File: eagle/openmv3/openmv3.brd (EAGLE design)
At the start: 35.6 x 44.5 mm, 60 parts, among them Q1 MOSFET, U1 STM32F765VGT6, U2 OV7725, U3 BD33IA, X1 47571-0001, X2 MICROUSB-RIGHT, Y1 7S-12.000MAHE-T

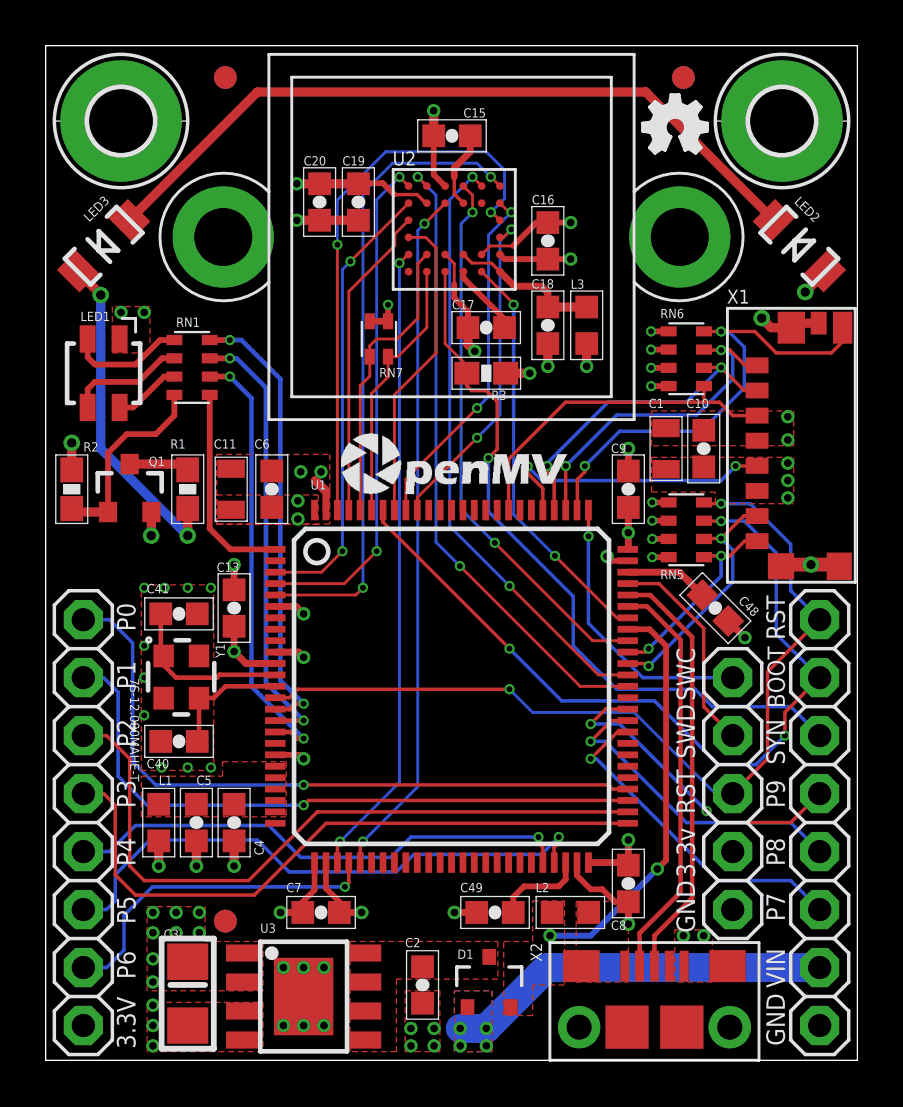
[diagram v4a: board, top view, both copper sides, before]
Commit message: Update OMV3 Eagle files.
* Add 22uF for the uSD
* Add 22uf for reg input
* Add 47uF near the MCU
* Add 47uF near the sensor
* Add 22uF for sensor digital input
* Replace sensor bead with RC filter on AVDD
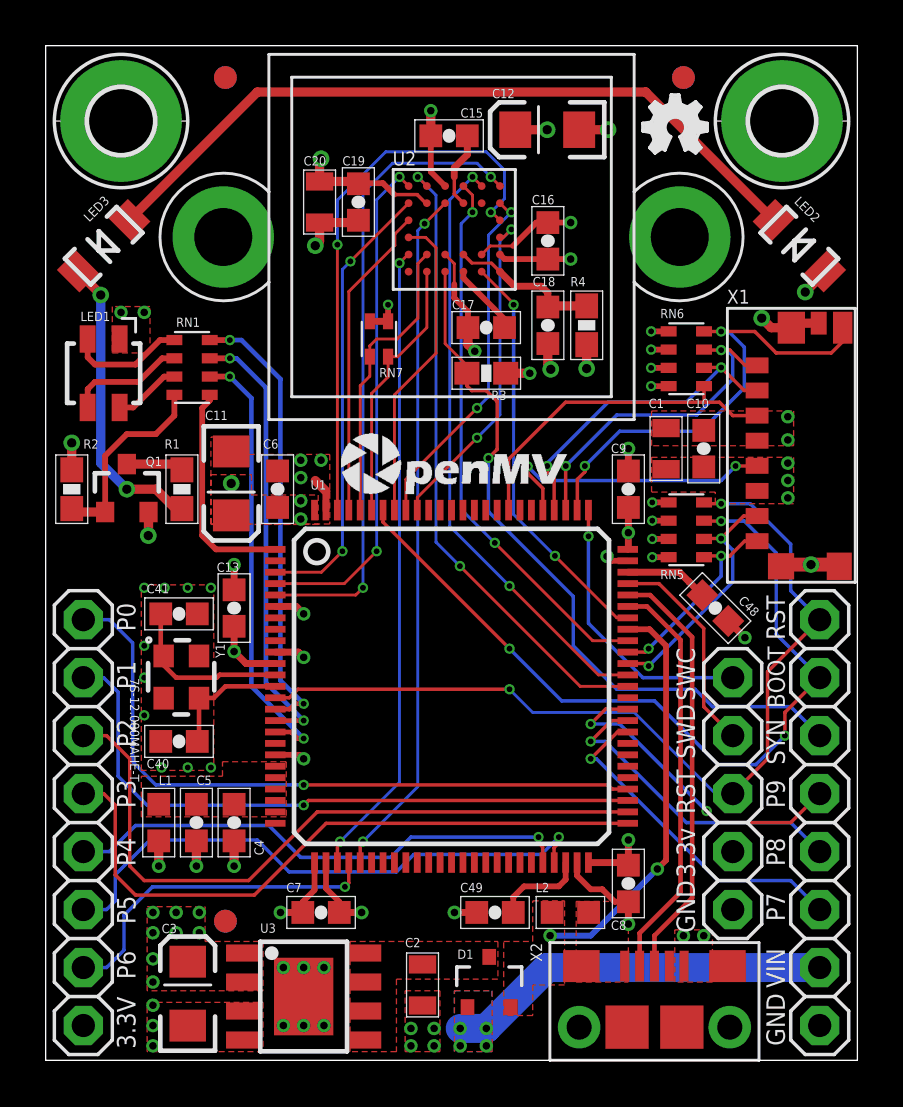
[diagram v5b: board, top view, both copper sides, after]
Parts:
- removed L3: MPZ1608S181ATAH0, sfe:0603
- added C12: 47uF, sfe:EIA3216
- added R4: 4.7R, sfe:0603-RES
- C11: value 22uF -> 47uF; device sfe:0805 -> sfe:EIA3216
- C18: value 0.1uF -> 4.7uF
- C2, C20: value 4.7uF -> 22uF; device sfe:0603-CAP -> sfe:0805
- C3: device sfe:1206 -> sfe:EIA3216
- moved C11 0.25 mm to (8.13, 25.3)
- moved C6 0.25 mm to (10.2, 25.0)
- moved R1 0.25 mm to (5.97, 25.0)
- moved C15 0.13 mm to (17.7, 40.5)
- moved Q1 0.13 mm to (3.56, 25.0)
- turned C3 to 90 degrees
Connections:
- net GND: now also C11.C, C12.C, C3.C; no longer C11.1, C3.2
- net N$13: now also R4.1; no longer L3.1
- net VCC: now also C11.A, C12.A, C3.A, R4.2; no longer C11.2, C3.1, L3.2
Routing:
- net GND: track 45.0 -> 46.6 mm, vias 52 -> 54
- net N$10: track 14.7 -> 13.2 mm
- net VCC: track 29.0 -> 30.4 mm, vias 31 -> 33
- net LED_IR: track 9.11 -> 9.76 mm

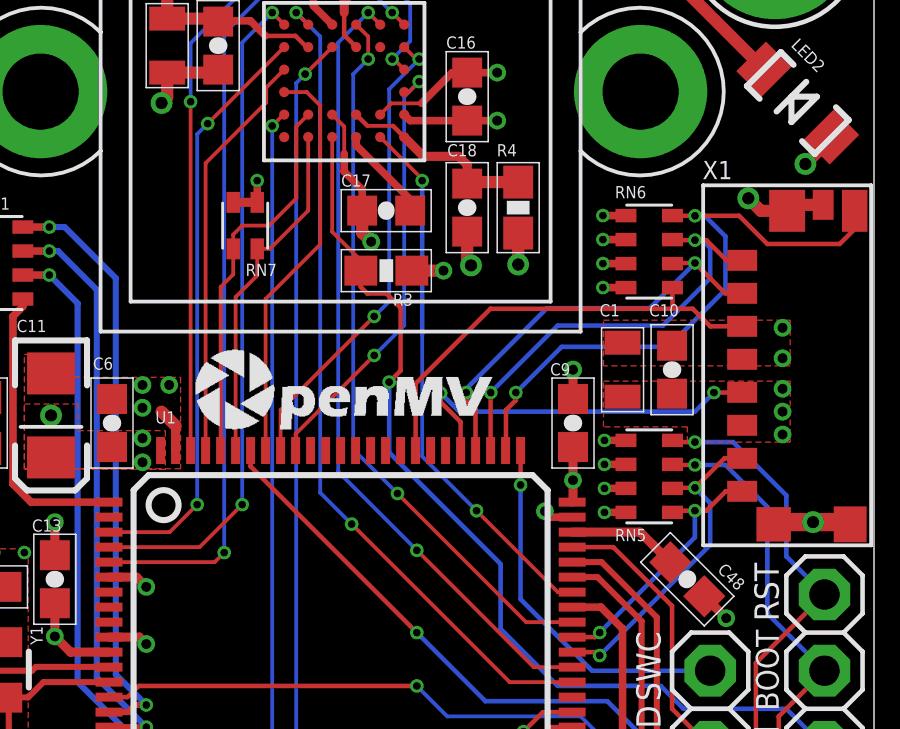
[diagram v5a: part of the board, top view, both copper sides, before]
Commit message: Update OMV3 Eagle Files.
* Fix some parts names.
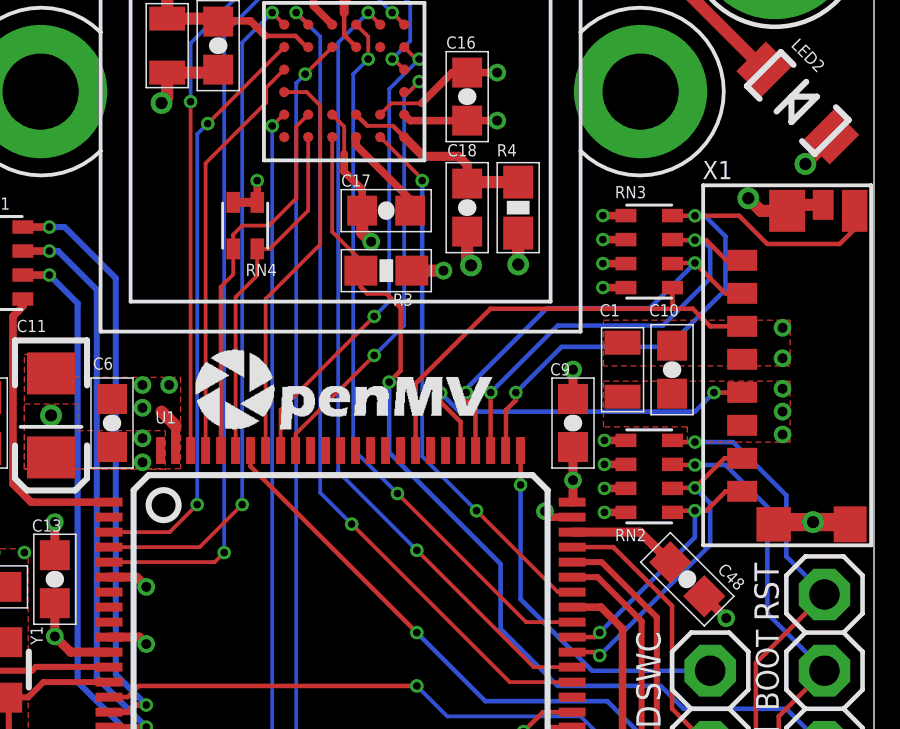
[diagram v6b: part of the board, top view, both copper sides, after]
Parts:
- R1: value 5ohm -> 10R
- RN4: value 10K -> 4.7K
- X2: value MICROUSB-RIGHT -> MF-CON-MICROUSB-RIGHT
- renumbered RN5 to RN2, RN6 to RN3, RN7 to RN4
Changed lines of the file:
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@@
 <element name="LM1" library="omnivision" package="LENSMOUNT-20MM" value="LENSMOUNT20MM" x="17.78" y="36.068" smashed="yes"/>
 <element name="H1" library="holes" package="2,8-PAD" value="MOUNT-PAD-ROUND2.8" x="3.302" y="41.148" smashed="yes" rot="R90"/>
-<element name="RN6" library="resistor-dil" package="EXBV8V" value="10K" x="28.067" y="30.734" smashed="yes" rot="R270">
+<element name="RN3" library="resistor-dil" package="EXBV8V" value="10K" x="28.067" y="30.734" smashed="yes" rot="R270">
 <attribute name="OC_NEWARK" value="unknown" x="28.067" y="30.734" size="1.778" layer="27" rot="R270" display="off"/>
 <attribute name="MPN" value="" x="28.067" y="30.734" size="1.778" layer="27" rot="R270" display="off"/>
@@
 <attribute name="VALUE" x="29.337" y="32.639" size="0.4064" layer="27" font="vector" ratio="20" rot="R270"/>
 </element>
-<element name="RN5" library="resistor-dil" package="EXBV8V" value="10K" x="28.067" y="23.241" smashed="yes" rot="R270">
+<element name="RN2" library="resistor-dil" package="EXBV8V" value="10K" x="28.067" y="23.241" smashed="yes" rot="R270">
 <attribute name="OC_NEWARK" value="unknown" x="28.067" y="23.241" size="1.778" layer="27" rot="R270" display="off"/>
 <attribute name="MPN" value="" x="28.067" y="23.241" size="1.778" layer="27" rot="R270" display="off"/>
@@
 <attribute name="VALUE" x="2.54" y="24.8285" size="0.4064" layer="27" font="vector" ratio="20"/>
 </element>
-<element name="RN7" library="resistor-dil" package="EXBV4V" value="10K" x="14.6" y="31.6" smashed="yes">
+<element name="RN4" library="resistor-dil" package="EXBV4V" value="4.7K" x="14.6" y="31.6" smashed="yes">
 <attribute name="OC_NEWARK" value="unknown" x="14.6" y="31.6" size="1.778" layer="27" display="off"/>
 <attribute name="MPN" value="" x="14.6" y="31.6" size="1.778" layer="27" display="off"/>
@@
 <attribute name="VALUE" x="25.781" y="27.813" size="0.4064" layer="27" rot="R270"/>
 </element>
-<element name="R1" library="sfe" package="0603-RES" value="5ohm" x="5.969" y="25.019" smashed="yes" rot="R270">
+<element name="R1" library="sfe" package="0603-RES" value="10R" x="5.969" y="25.019" smashed="yes" rot="R270">
 <attribute name="NAME" x="5.207" y="26.797" size="0.4064" layer="25" font="vector" ratio="20"/>
 <attribute name="VALUE" x="4.826" y="26.0985" size="0.4064" layer="27" rot="R270"/>
@@
 <attribute name="VALUE" x="12.645" y="15.288" size="1.27" layer="27"/>
 </element>
-<element name="X2" library="MF_Connectors" package="MICROUSB-RIGHT" value="MICROUSB-RIGHT" x="26.67" y="2.8575" smashed="yes">
+<element name="X2" library="MF_Connectors" package="MICROUSB-RIGHT" value="MF-CON-MICROUSB-RIGHT" x="26.67" y="2.8575" smashed="yes">
 <attribute name="NAME" x="21.7475" y="4.318" size="0.508" layer="25" font="vector" ratio="16" rot="R90"/>
 </element>
@@
 <via x="11.303" y="13.208" extent="1-16" drill="0.3302"/>
 <contactref element="JP3" pad="5"/>
-<contactref element="RN5" pad="2"/>
+<contactref element="RN2" pad="2"/>
 <wire x1="27.292" y1="23.641" x2="26.5746" y2="23.641" width="0.254" layer="1"/>
 <via x="26.5746" y="23.641" extent="1-16" drill="0.254"/>
@@
 <wire x1="21.336" y1="15.24" x2="20.32" y2="16.256" width="0.127" layer="16"/>
 <contactref element="JP1" pad="1"/>
-<contactref element="RN5" pad="8"/>
+<contactref element="RN2" pad="8"/>
 <wire x1="28.842" y1="24.441" x2="28.899" y2="24.384" width="0.1524" layer="1"/>
 <wire x1="28.899" y1="24.384" x2="29.591" y2="24.384" width="0.1524" layer="1"/>
@@
 <contactref element="U1" pad="94"/>
 <contactref element="JP1" pad="2"/>
-<contactref element="RN5" pad="7"/>
+<contactref element="RN2" pad="7"/>
 <wire x1="28.842" y1="23.641" x2="28.861" y2="23.622" width="0.1524" layer="1"/>
 <wire x1="28.861" y1="23.622" x2="29.591" y2="23.622" width="0.1524" layer="1"/>
@@
 <contactref element="C13" pad="1"/>
 <contactref element="C10" pad="1"/>
-<contactref element="RN6" pad="1"/>
-<contactref element="RN6" pad="2"/>
-<contactref element="RN6" pad="3"/>
-<contactref element="RN6" pad="4"/>
-<contactref element="RN5" pad="4"/>
+<contactref element="RN3" pad="1"/>
+<contactref element="RN3" pad="2"/>
+<contactref element="RN3" pad="3"/>
+<contactref element="RN3" pad="4"/>
+<contactref element="RN2" pad="4"/>
 <contactref element="L1" pad="2"/>
 <contactref element="X1" pad="P$4"/>
@@
 </polygon>
 <contactref element="LED1" pad="A"/>
-<contactref element="RN7" pad="3"/>
-<contactref element="RN7" pad="4"/>
+<contactref element="RN4" pad="3"/>
+<contactref element="RN4" pad="4"/>
 <contactref element="C1" pad="1"/>
 <via x="11.303" y="19.558" extent="1-16" drill="0.3302"/>
@@
 <via x="25.527" y="23.114" extent="1-16" drill="0.3302"/>
 <contactref element="JP2" pad="8"/>
-<contactref element="RN5" pad="3"/>
+<contactref element="RN2" pad="3"/>
 <polygon width="0.1524" layer="1" isolate="0.254" thermals="no">
 <vertex x="26.543" y="28.448"/>
@@
 <wire x1="12.28" y1="7.532" x2="12.865" y2="6.947" width="0.254" layer="1"/>
 <wire x1="12.865" y1="6.477" x2="12.865" y2="6.947" width="0.254" layer="1"/>
-<contactref element="RN5" pad="1"/>
+<contactref element="RN2" pad="1"/>
 <wire x1="27.292" y1="24.441" x2="26.5746" y2="24.441" width="0.254" layer="1"/>
 <wire x1="27.292" y1="22.841" x2="26.5746" y2="22.841" width="0.254" layer="1"/>
@@
 <signal name="SD_CD">
 <contactref element="X1" pad="G$5"/>
-<contactref element="RN6" pad="8"/>
+<contactref element="RN3" pad="8"/>
 <via x="29.591" y="31.9278" extent="1-16" drill="0.254"/>
 <wire x1="23.2918" y1="24.1148" x2="23.28" y2="24.103" width="0.1524" layer="1" curve="-90"/>
@@
 <signal name="SDIO_D0">
 <contactref element="X1" pad="P$7"/>
-<contactref element="RN5" pad="6"/>
+<contactref element="RN2" pad="6"/>
 <via x="29.591" y="22.86" extent="1-16" drill="0.254"/>
 <wire x1="29.591" y1="22.86" x2="28.861" y2="22.86" width="0.1524" layer="1"/>
@@
 <signal name="SDIO_D1">
 <contactref element="X1" pad="P$8"/>
-<contactref element="RN5" pad="5"/>
+<contactref element="RN2" pad="5"/>
 <via x="29.591" y="22.098" extent="1-16" drill="0.254"/>
 <wire x1="28.899" y1="22.098" x2="28.842" y2="22.041" width="0.2032" layer="1"/>
@@
 <signal name="SDIO_D2">
 <contactref element="X1" pad="P$1"/>
-<contactref element="RN6" pad="7"/>
+<contactref element="RN3" pad="7"/>
 <wire x1="22.7838" y1="24.1068" x2="22.78" y2="24.103" width="0.1524" layer="1" curve="-90"/>
 <wire x1="28.8484" y1="31.1404" x2="28.842" y2="31.134" width="0.1524" layer="1" curve="90"/>
@@
 <signal name="SDIO_CMD">
 <contactref element="X1" pad="P$3"/>
-<contactref element="RN6" pad="5"/>
+<contactref element="RN3" pad="5"/>
 <wire x1="20.28" y1="24.103" x2="20.28" y2="26.333" width="0.1524" layer="1"/>
 <wire x1="29.518" y1="28.829" x2="30.104" y2="28.243" width="0.1524" layer="1"/>
@@
 <signal name="SDIO_D3">
 <contactref element="X1" pad="P$2"/>
-<contactref element="RN6" pad="6"/>
+<contactref element="RN3" pad="6"/>
 <wire x1="22.2758" y1="24.1072" x2="22.28" y2="24.103" width="0.1524" layer="1" curve="90"/>
 <wire x1="28.8484" y1="30.3276" x2="28.842" y2="30.334" width="0.1524" layer="1" curve="-90"/>
@@
 </signal>
 <signal name="I2C1_SCL">
-<contactref element="RN7" pad="2"/>
+<contactref element="RN4" pad="2"/>
 <contactref element="U2" pad="A5"/>
 <wire x1="14.28" y1="24.103" x2="14.28" y2="29.217" width="0.127" layer="1"/>
@@
 </signal>
 <signal name="I2C1_SDA">
-<contactref element="RN7" pad="1"/>
+<contactref element="RN4" pad="1"/>
 <contactref element="U2" pad="B5"/>
 <wire x1="13.78" y1="24.103" x2="13.78" y2="29.552" width="0.127" layer="1"/>
